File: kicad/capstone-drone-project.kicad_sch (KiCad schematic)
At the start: 23 parts, among them Q1 PMOS, Q2 PMOS, Q3 NMOS, U1 ESP32-S3, Y1 ECS-400-10-37B2-CKY-TR

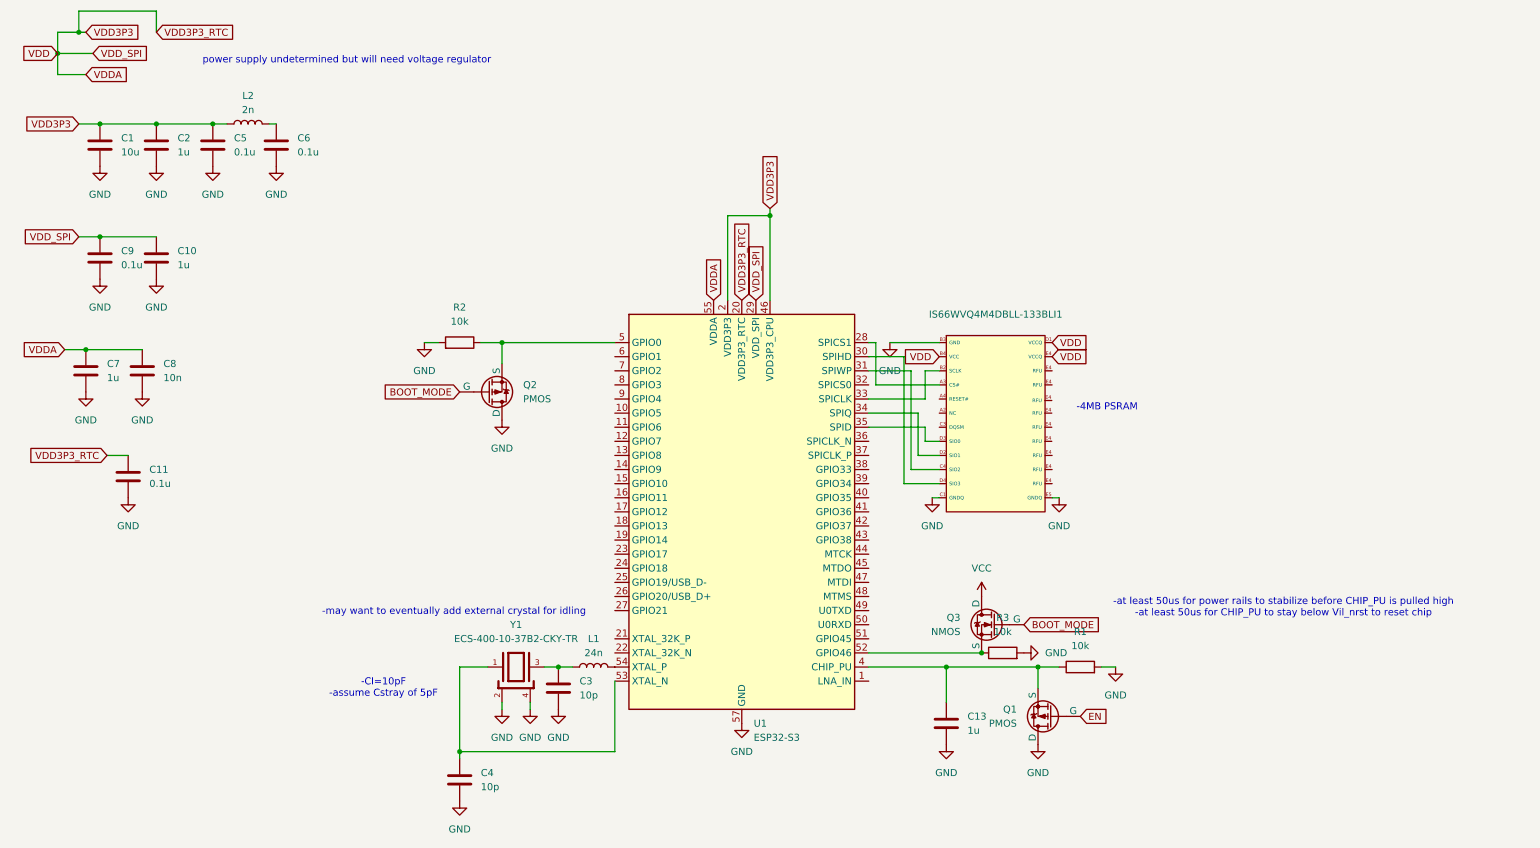
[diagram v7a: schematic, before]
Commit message: outlining rf matching circuits
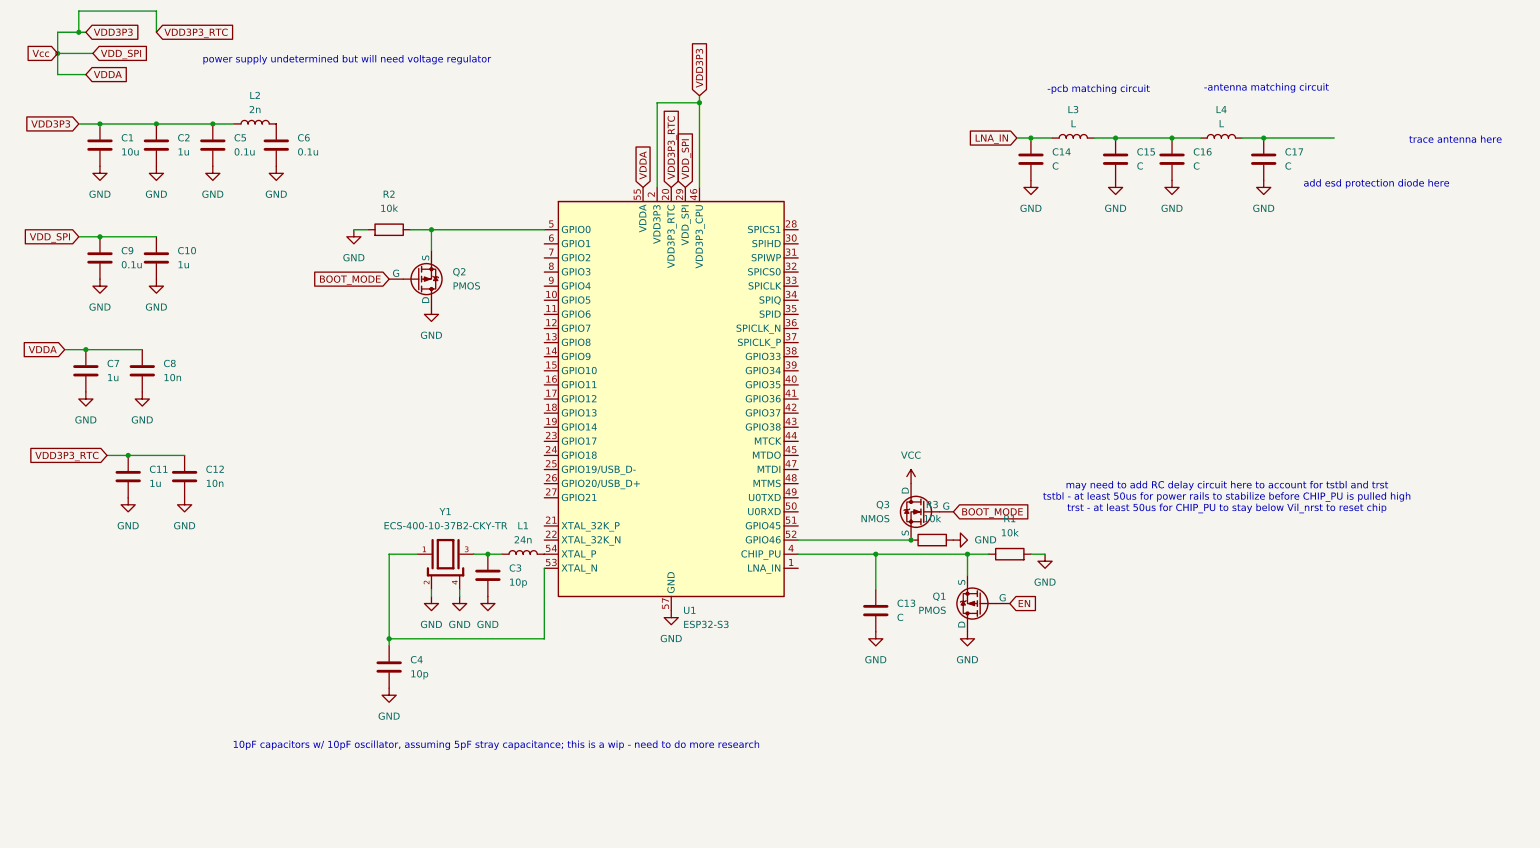
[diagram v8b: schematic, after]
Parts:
- removed IS66WVQ4M4DBLL-133BLI1: ~, symbol capstone-drone-project-library:IS66WVQ4M4DBLL-133BLI
- added C12: 10n, symbol Device:C
- added C14, C15, C16, C17: C, symbol Device:C
- added L3, L4: L, symbol Device:L
- C11: value 0.1u -> 1u
- C13: value 1u -> C
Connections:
- net GND: now also C12.2, C14.2, C15.2, C16.2, C17.2
- net VDD  renamed VDD3P3
- net VDD3P3: now also C12.1
- new net: C15.1, C16.1, L3.2, L4.1
- new net: C17.1, L4.2
- new net LNA_IN: C14.1, L3.1
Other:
- note added: "-antenna matching circuit"
- note added: "-pcb matching circuit"
- note added: "10pF capacitors w/ 10pF oscillator, assuming 5pF stray capacitance; this is a wip - need to do more research"
- note added: "add esd protection diode here"
- note added: "may need to add RC delay circuit here to account for tstbl and trst tstbl - at least 50us for power rails to stabilize before CHIP_PU is pulled high trst - at least 50us for CHIP_PU to stay below Vil_nrst to reset chip"
- note added: "trace antenna here"
- note removed: "-4MB PSRAM"
- note removed: "-Cl=10pF -assume Cstray of 5pF"
- note removed: "-at least 50us for power rails to stabilize before CHIP_PU is pulled high -at least 50us for CHIP_PU to stay below Vil_nrst to reset chip"
- note removed: "-may want to eventually add external crystal for idling"
- moved on the sheet: C13, C3, C4, L1, L2, Q1, Q2, Q3, R1, R2, R3, U1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
